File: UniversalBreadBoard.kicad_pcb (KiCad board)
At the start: 2 copper layers, 78.7 x 53.3 mm, 80 parts, among them J1 Conn_01x06_Pin, J10 Conn_01x06_Pin, J11 Conn_01x06_Pin, J12 Conn_01x06_Pin, J13 Conn_01x06_Pin, J14 Conn_01x06_Pin, J15 Conn_01x06_Pin, J16 Conn_01x06_Pin, J17 Conn_01x06_Pin, J18 Conn_01x06_Pin, J19 Conn_01x06_Pin, J2 Conn_01x06_Pin, J20 Conn_01x06_Pin, J21 Conn_01x06_Pin, J22 Conn_01x06_Pin, J23 Conn_01x06_Pin, J24 Conn_01x06_Pin, J25 Conn_01x06_Pin, J26 Conn_01x06_Pin, J27 Conn_01x06_Pin, J28 Conn_01x06_Pin, J29 Conn_01x06_Pin, J3 Conn_01x06_Pin, J30 Conn_01x06_Pin, J31 Conn_01x06_Pin, J32 Conn_01x06_Pin, J33 Conn_01x06_Pin, J34 Conn_01x06_Pin, J35 Conn_01x06_Pin, J36 Conn_01x06_Pin, J37 Conn_01x06_Pin, J38 Conn_01x06_Pin, J39 Conn_01x06_Pin, J4 Conn_01x06_Pin, J40 Conn_01x06_Pin, J41 Conn_01x06_Pin, J42 Conn_01x06_Pin, J43 Conn_01x06_Pin, J44 Conn_01x06_Pin, J45 Conn_01x06_Pin, J46 Conn_01x06_Pin, J47 Conn_01x06_Pin, J48 Conn_01x06_Pin, J49 Conn_01x06_Pin, J5 Conn_01x06_Pin, J50 Conn_01x06_Pin, J51 Conn_01x06_Pin, J52 Conn_01x06_Pin, J53 Conn_01x06_Pin, J54 Conn_01x06_Pin, J55 Conn_01x06_Pin, J56 Conn_01x06_Pin, J57 Conn_01x06_Pin, J58 Conn_01x06_Pin, J59 Conn_01x06_Pin, J6 Conn_01x06_Pin, J60 Conn_01x06_Pin, J61 Conn_01x06_Pin, J62 Conn_01x06_Pin, J63 Conn_01x06_Pin, J64 Conn_01x06_Pin, J65 Conn_01x06_Pin, J66 Conn_01x06_Pin, J67 Conn_01x06_Pin, J68 Conn_01x06_Pin, J69 Conn_01x06_Pin, J7 Conn_01x06_Pin, J70 Conn_01x06_Pin, J71 Conn_01x06_Pin, J72 Conn_01x06_Pin, J73 Conn_01x06_Pin, J74 Conn_01x06_Pin, J75 Conn_01x06_Pin, J76 Conn_01x06_Pin, J77 Conn_01x06_Pin, J78 Conn_01x06_Pin, J79 Conn_01x06_Pin, J8 Conn_01x06_Pin, J80 Conn_01x06_Pin, J9 Conn_01x06_Pin

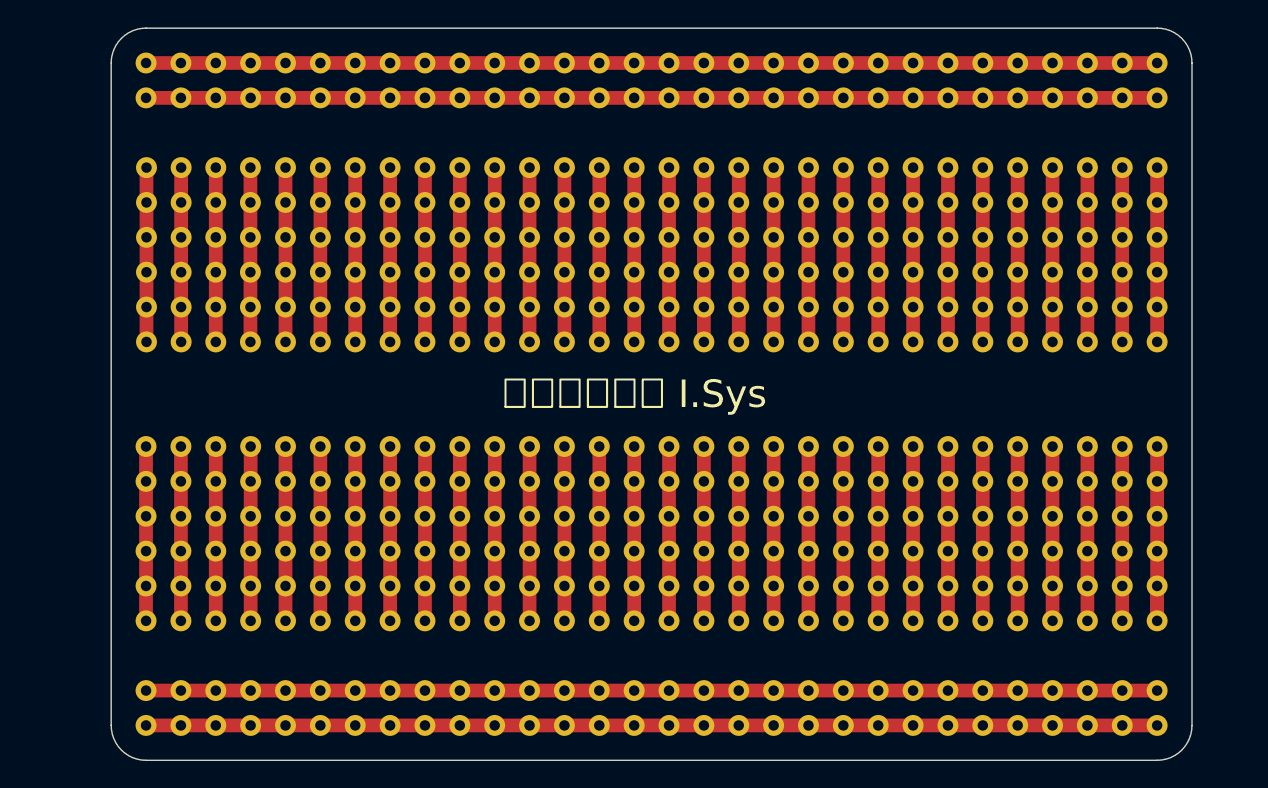
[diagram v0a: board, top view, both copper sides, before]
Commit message: v2 update
行・列の刻印を追加
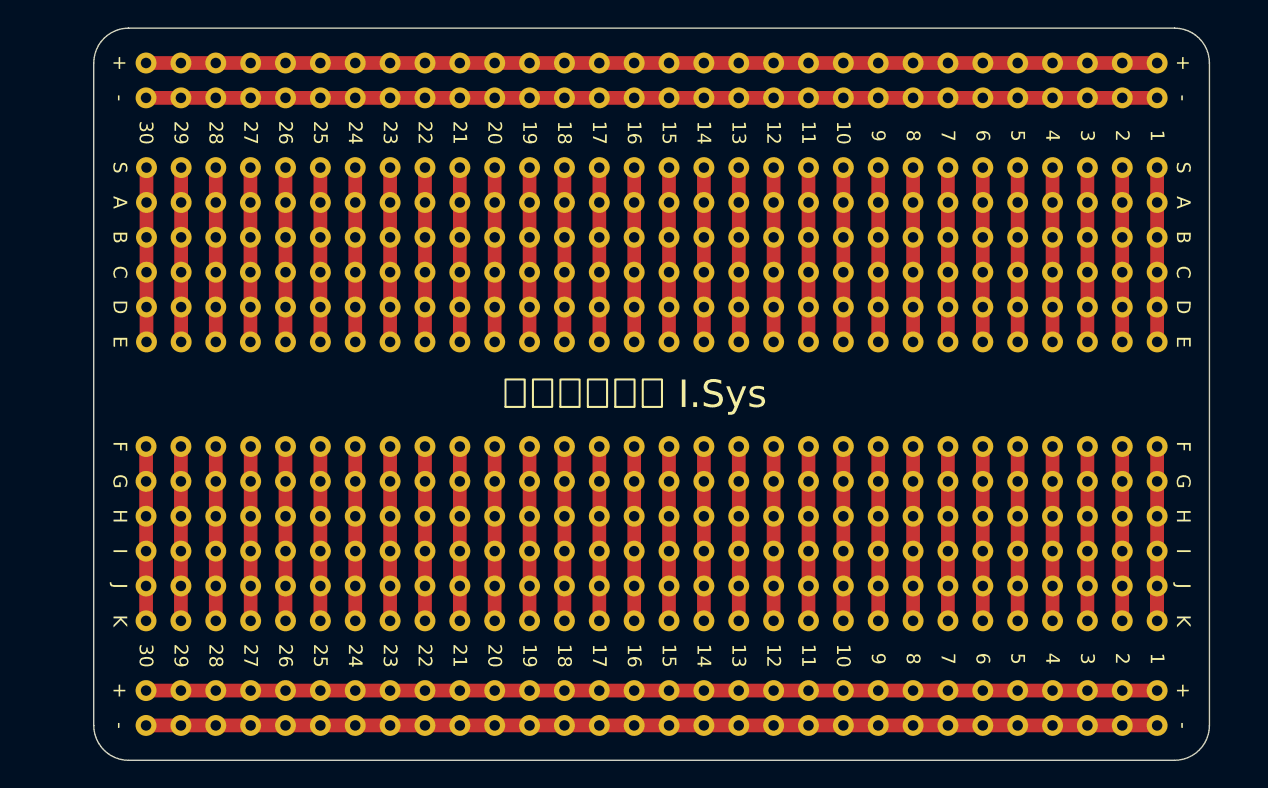
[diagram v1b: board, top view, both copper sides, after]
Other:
- board size 78.7 x 53.3 mm -> 81.3 x 53.3 mm
- board text added: "+"
- board text added: "-"
- board text added: "1"
- board text added: "10"
- board text added: "11"
- board text added: "12"
- board text added: "13"
- board text added: "14"
- board text added: "15"
- board text added: "16"
- board text added: "17"
- board text added: "18"
- board text added: "19"
- board text added: "2"
- board text added: "20"
- board text added: "21"
- board text added: "22"
- board text added: "23"
- board text added: "24"
- board text added: "25"
- board text added: "26"
- board text added: "27"
- board text added: "28"
- board text added: "29"
- board text added: "3"
- board text added: "30"
- board text added: "4"
- board text added: "5"
- board text added: "6"
- board text added: "7"
- board text added: "8"
- board text added: "9"
- board text added: "A"
- board text added: "B"
- board text added: "C"
- board text added: "D"
- board text added: "E"
- board text added: "F"
- board text added: "G"
- board text added: "H"
- board text added: "I"
- board text added: "J"
- board text added: "K"
- board text added: "S"

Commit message: 縦方向，中央の刻印を編集
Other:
- board text added: "L"
- board text added: "からくり工房 I.Sys - ブレッドボード風ユニバーサル基板"
- board text removed: "からくり工房 I.Sys"
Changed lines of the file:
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@@
     (effects (font (size 1 1) (thickness 0.15)))
   )
-  (gr_text "I" (at 184.785 124.46 270) (layer "F.SilkS")
+  (gr_text "I" (at 184.785 121.92 270) (layer "F.SilkS")
     (effects (font (size 1 1) (thickness 0.15)))
   )
@@
     (effects (font (size 1 1) (thickness 0.15)))
   )
-  (gr_text "からくり工房 I.Sys" (at 144.78 113.03) (layer "F.SilkS")
+  (gr_text "からくり工房 I.Sys - ブレッドボード風ユニバーサル基板" (at 144.78 113.03) (layer "F.SilkS")
     (effects (font (size 2 2) (thickness 0.15)))
   )
@@
     (effects (font (size 1 1) (thickness 0.15)))
   )
-  (gr_text "B" (at 184.785 101.6 270) (layer "F.SilkS")
+  (gr_text "B" (at 184.785 99.06 270) (layer "F.SilkS")
     (effects (font (size 1 1) (thickness 0.15)))
   )
@@
     (effects (font (size 1 1) (thickness 0.15)))
   )
-  (gr_text "K" (at 184.785 129.54 270) (layer "F.SilkS")
+  (gr_text "K" (at 184.785 127 270) (layer "F.SilkS")
     (effects (font (size 1 1) (thickness 0.15)))
   )
@@
     (effects (font (size 1 1) (thickness 0.15)))
   )
+  (gr_text "L" (at 184.785 129.54 270) (layer "F.SilkS")
+    (effects (font (size 1 1) (thickness 0.15)))
+  )
   (gr_text "H" (at 107.315 121.92 270) (layer "F.SilkS")
     (effects (font (size 1 1) (thickness 0.15)))
@@
     (effects (font (size 1 1) (thickness 0.15)))
   )
-  (gr_text "C" (at 184.785 104.14 270) (layer "F.SilkS")
+  (gr_text "C" (at 184.785 101.6 270) (layer "F.SilkS")
     (effects (font (size 1 1) (thickness 0.15)))
   )
@@
     (effects (font (size 1 1) (thickness 0.15)))
   )
-  (gr_text "S" (at 184.785 96.52 270) (layer "F.SilkS")
-    (effects (font (size 1 1) (thickness 0.15)))
-  )
   (gr_text "-" (at 107.315 91.44 270) (layer "F.SilkS")
     (effects (font (size 1 1) (thickness 0.15)))
@@
     (effects (font (size 1 1) (thickness 0.15)))
   )
-  (gr_text "A" (at 184.785 99.06 270) (layer "F.SilkS")
-    (effects (font (size 1 1) (thickness 0.15)))
-  )
-  (gr_text "E" (at 184.785 109.22 270) (layer "F.SilkS")
-    (effects (font (size 1 1) (thickness 0.15)))
-  )
-  (gr_text "G" (at 184.785 119.38 270) (layer "F.SilkS")
+  (gr_text "A" (at 184.785 96.52 270) (layer "F.SilkS")
+    (effects (font (size 1 1) (thickness 0.15)))
+  )
+  (gr_text "E" (at 184.785 106.68 270) (layer "F.SilkS")
+    (effects (font (size 1 1) (thickness 0.15)))
+  )
+  (gr_text "G" (at 184.785 116.84 270) (layer "F.SilkS")
     (effects (font (size 1 1) (thickness 0.15)))
   )
@@
     (effects (font (size 1 1) (thickness 0.15)))
   )
-  (gr_text "H" (at 184.785 121.92 270) (layer "F.SilkS")
+  (gr_text "H" (at 184.785 119.38 270) (layer "F.SilkS")
     (effects (font (size 1 1) (thickness 0.15)))
   )
@@
     (effects (font (size 1 1) (thickness 0.15)))
   )
-  (gr_text "D" (at 184.785 106.68 270) (layer "F.SilkS")
+  (gr_text "D" (at 184.785 104.14 270) (layer "F.SilkS")
     (effects (font (size 1 1) (thickness 0.15)))
   )
@@
     (effects (font (size 1 1) (thickness 0.15)))
   )
-  (gr_text "F" (at 184.785 116.84 270) (layer "F.SilkS")
+  (gr_text "F" (at 184.785 109.22 270) (layer "F.SilkS")
     (effects (font (size 1 1) (thickness 0.15)))
   )
@@
     (effects (font (size 1 1) (thickness 0.15)))
   )
-  (gr_text "J" (at 184.785 127 270) (layer "F.SilkS")
-    (effects (font (size 1 1) (thickness 0.15)))
-  )
+  (gr_text "J" (at 184.785 124.46 270) (layer "F.SilkS")
+    (effects (font (size 1 1) (thickness 0.15)))
+  )
